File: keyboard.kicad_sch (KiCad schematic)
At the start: 1 part

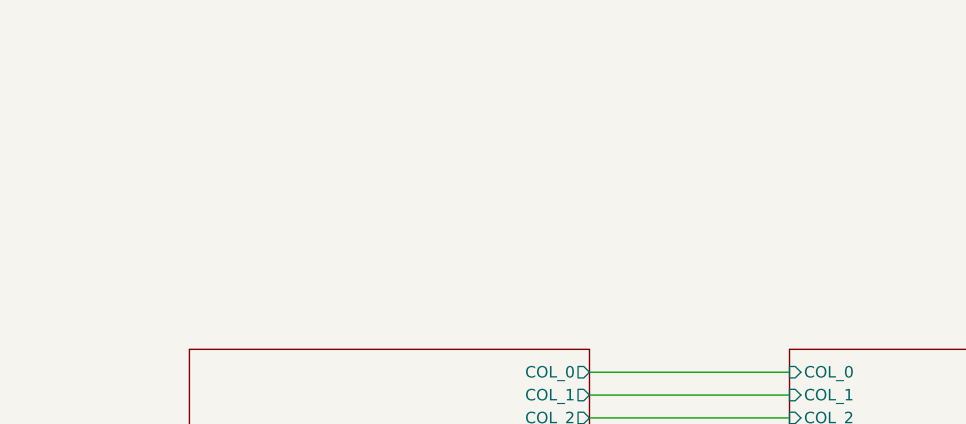
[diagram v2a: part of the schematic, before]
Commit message: updated library references to local
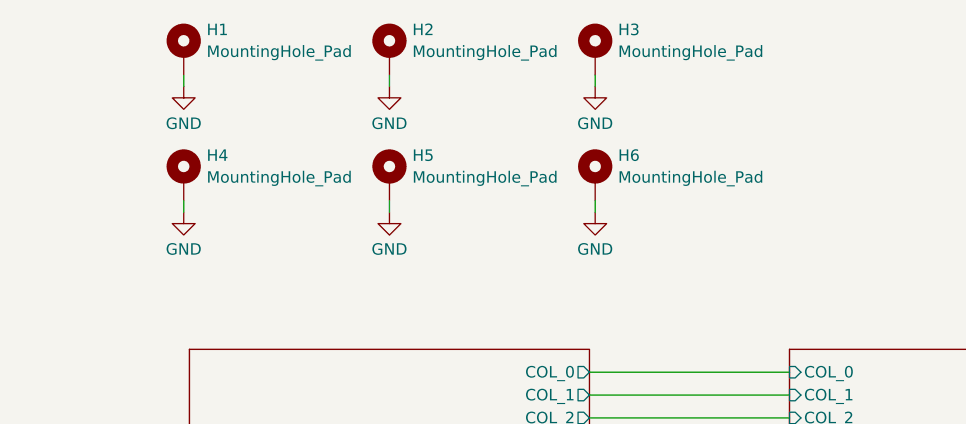
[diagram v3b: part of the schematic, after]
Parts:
- added H1, H2, H3, H4, H5, H6: MountingHole_Pad, MountingHole:MountingHole_3.2mm_M3_Pad, symbol Mechanical:MountingHole_Pad
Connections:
- new net GND: H1.1, H2.1, H3.1, H4.1, H5.1, H6.1
